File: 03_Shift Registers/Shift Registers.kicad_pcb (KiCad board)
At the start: 2 copper layers, 100 x 100 mm, 51 parts, among them J1 Data bus, J2 Alu-X bus, J3 Alu-Y bus, J4 Input 1, J5 Input 2, U1 74LS194, U10 74LS245, U2 74LS245, U3 74LS194, U4 74LS194, U5 74LS245, U6 74LS194, U7 74LS245, U8 74LS245, U9 74LS245

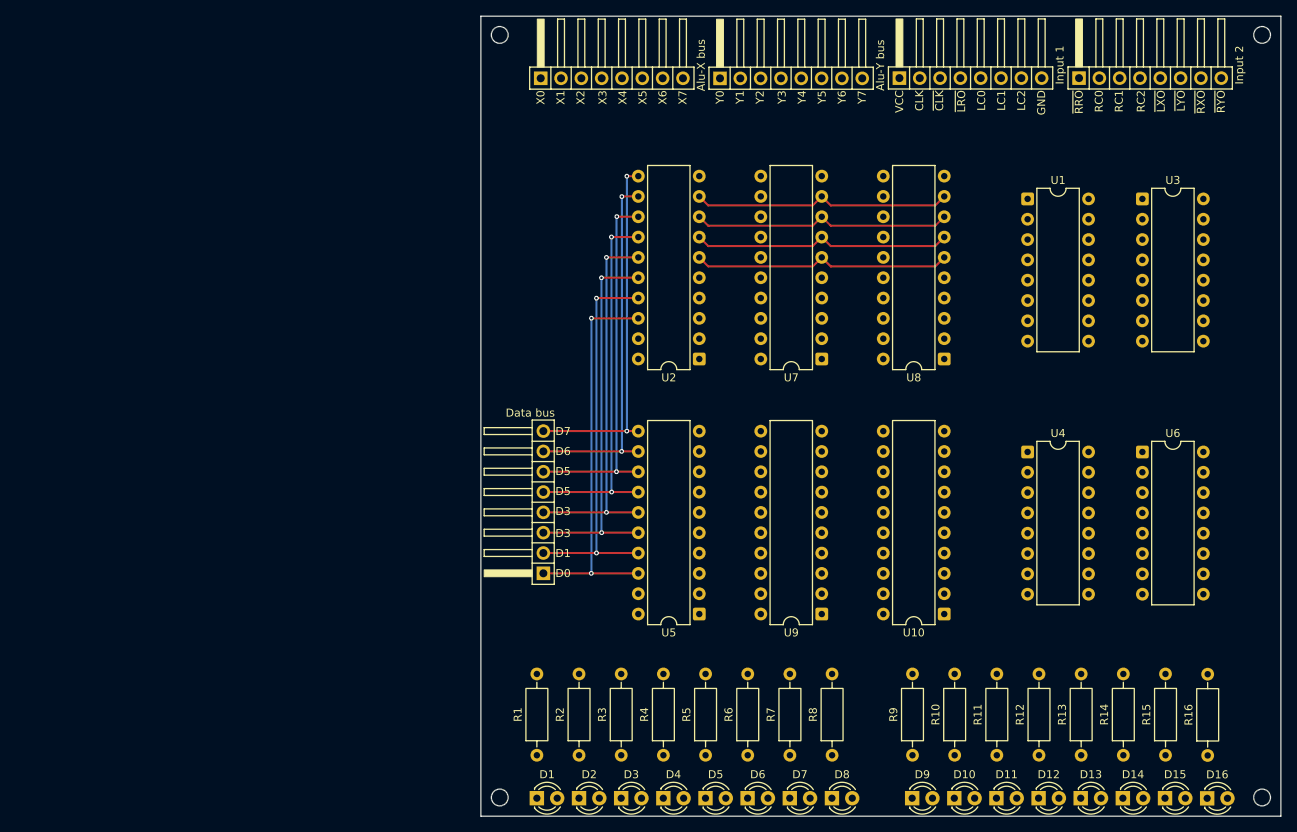
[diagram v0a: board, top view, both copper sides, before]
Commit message: Alu control and modules completed, as well as Stack pointer module
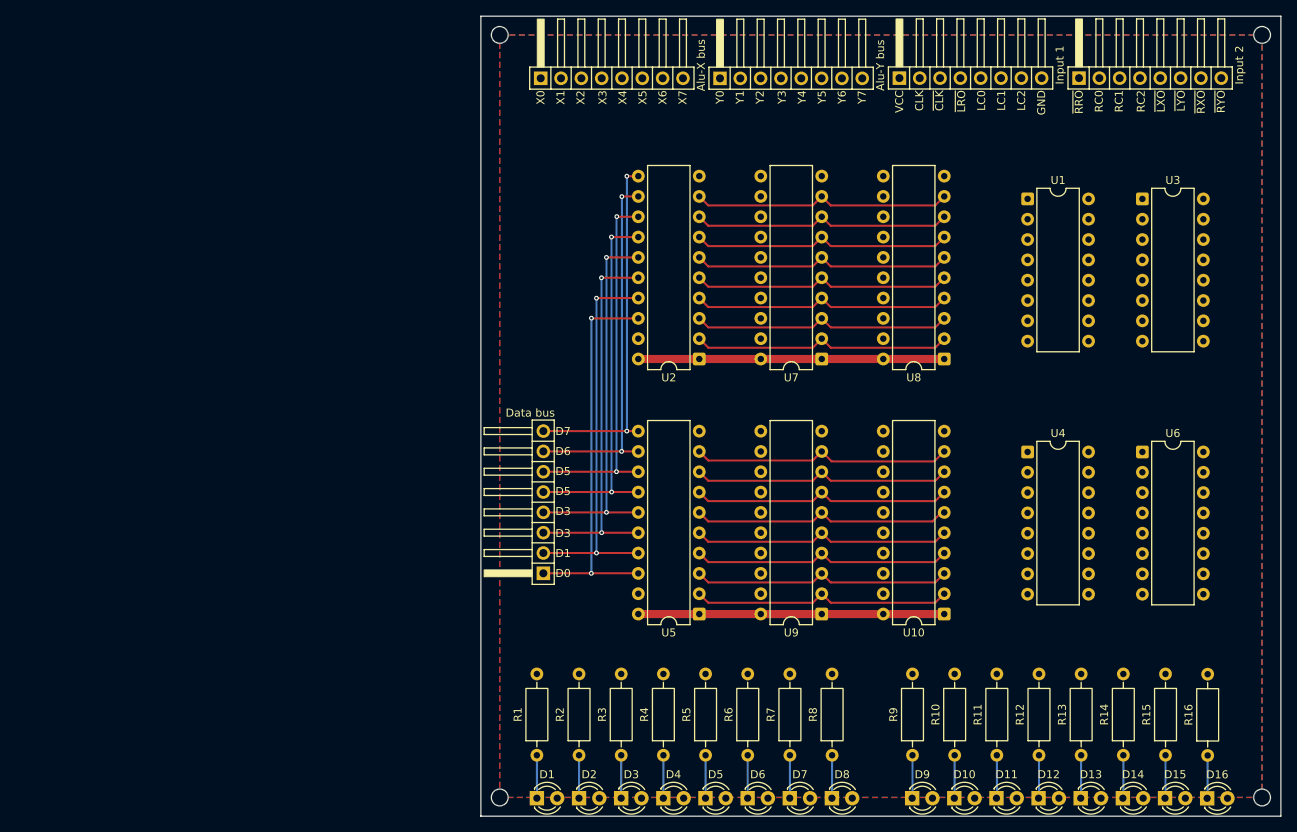
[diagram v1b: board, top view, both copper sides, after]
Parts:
- D1, D10, D11, D12, D13, D14, D15, D16, D2, D3, D4, D5, D6, D7, D8, D9: value LED -> RED
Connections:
- net /CLK renamed CLK
- net /D0 renamed D0
- net /D1 renamed D1
- net /D2 renamed D2
- net /D3 renamed D3
- net /D4 renamed D4
- net /D5 renamed D5
- net /D6 renamed D6
- net /D7 renamed D7
- net /GND renamed GND
- net /LC0 renamed LC0
- net /LC1 renamed LC1
- net /LC2 renamed LC2
- net /RC0 renamed RC0
- net /RC1 renamed RC1
- net /RC2 renamed RC2
- net /VCC renamed VCC
- net /X0 renamed X0
- net /X1 renamed X1
- net /X2 renamed X2
- net /X3 renamed X3
- net /X4 renamed X4
- net /X5 renamed X5
- net /X6 renamed X6
- net /X7 renamed X7
- net /Y0 renamed Y0
- net /Y1 renamed Y1
- net /Y2 renamed Y2
- net /Y3 renamed Y3
- net /Y4 renamed Y4
- net /Y5 renamed Y5
- net /Y6 renamed Y6
- net /Y7 renamed Y7
- net /~{CLK} renamed ~{CLK}
- net /~{LRO} renamed ~{LRO}
- net /~{LXO} renamed ~{LXO}
- net /~{LYO} renamed ~{LYO}
- net /~{RRO} renamed ~{RRO}
- net /~{RXO} renamed ~{RXO}
- net /~{RYO} renamed ~{RYO}
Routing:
- net VCC: track 0.00 -> 76.5 mm
- net /Alu selector R-X/Q4: track 0.00 -> 33.0 mm
- net /Alu selector R-X/Q7: track 0.00 -> 32.6 mm
- net /Alu selector R-X/Q6: track 0.00 -> 32.5 mm
- net /Alu selector R-X/Q5: track 0.00 -> 32.5 mm
- net /Alu selector R-X/Q3: track 0.00 -> 32.5 mm
- net /Alu selector R-X/Q2: track 0.00 -> 32.5 mm
- net /Alu selector R-X/Q1: track 0.00 -> 32.5 mm
- net /Alu selector R-X/Q0: track 0.00 -> 32.5 mm
- net /Alu selector L-X/Q3: track 0.00 -> 32.5 mm
- net /Alu selector L-X/Q2: track 0.00 -> 32.5 mm
- net /Alu selector L-X/Q1: track 0.00 -> 32.5 mm
- net /Alu selector L-X/Q0: track 0.00 -> 32.5 mm
- net Net-(D15-K): track 0.00 -> 5.40 mm
- net Net-(D14-K): track 0.00 -> 5.39 mm
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- added copper zone on B.Cu, net GND
- added copper zone on F.Cu, net GND

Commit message: Last revision of the cpu, all boards have been ordered. Implementation to be tested and documented in following commits.
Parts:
- removed the U7 at (93.6, 86.0)
- removed the U9 at (93.6, 117.9)
- added U1: 74LS139, Package_DIP:DIP-16_W7.62mm, F.Cu at (19.2, 94.0)
- added U11: 74LS245, Package_DIP:DIP-20_W7.62mm, F.Cu at (6.47, 94.0)
- added U12: 74LS245, Package_DIP:DIP-20_W7.62mm, F.Cu at (-6.31, 65.1)
- added U13: 74LS245, Package_DIP:DIP-20_W7.62mm, F.Cu at (19.2, 65.1)
- U2: value 74LS245 -> 74LS00; footprint Package_DIP:DIP-20_W7.62mm -> Package_DIP:DIP-14_W7.62mm
- moved U10 117.7 mm to (-6.31, 94.0), turned to 0 degrees
- moved U5 89.1 mm to (6.47, 65.1), turned to 0 degrees
- moved U8 79.7 mm to (32.0, 65.1), turned to 0 degrees
- moved U2 48.9 mm to (30.0, 94.0), turned to 0 degrees
- renumbered R8 to R10, R9 to R11, R10 to R12, R11 to R13, R12 to R14, R13 to R15, R14 to R16, R15 to R17, R16 to R18, R1 to R3, R2 to R4, R3 to R5, R4 to R6, R5 to R7, R6 to R8, R7 to R9, U1 to U4, U3 to U6, U4 to U7, U6 to U9
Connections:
- J4 pad 7: LC2 -> LCL
- J5 pad 4: RC2 -> RCL
- U10 pad 11: Y7 -> X7
- U10 pad 12: Y6 -> X6
- U10 pad 13: Y5 -> X5
- U10 pad 14: Y4 -> X4
- U10 pad 15: Y3 -> X3
- U10 pad 16: Y2 -> X2
- U10 pad 17: Y1 -> X1
- U10 pad 18: Y0 -> X0
- U10 pad 19: ~{RYO} -> ~{LXO}
- U10 pad 2: /Alu selector R-X/Q0 -> /Alu selector L-X/Q0
- U10 pad 3: /Alu selector R-X/Q1 -> /Alu selector L-X/Q1
- U10 pad 4: /Alu selector R-X/Q2 -> /Alu selector L-X/Q2
- U10 pad 5: /Alu selector R-X/Q3 -> /Alu selector L-X/Q3
- U10 pad 6: /Alu selector R-X/Q4 -> /Alu selector L-X/Q4
- U10 pad 7: /Alu selector R-X/Q5 -> /Alu selector L-X/Q5
- U10 pad 8: /Alu selector R-X/Q6 -> /Alu selector L-X/Q6
- U10 pad 9: /Alu selector R-X/Q7 -> /Alu selector L-X/Q7
- U2 pad 1: VCC -> Net-(U1A-O1)
- U2 pad 10: GND -> ~{RRI}
- U2 pad 11: D7 -> /Shift register R/S1
- U2 pad 12: D6 -> ~{RRI}
- U2 pad 13: D5 -> Net-(U1B-O2)
- U2 pad 14: D4 -> VCC
- U2 pad 2: /Alu selector L-X/Q0 -> ~{LRI}
- U2 pad 3: /Alu selector L-X/Q1 -> /Shift register L/S0
- U2 pad 4: /Alu selector L-X/Q2 -> ~{LRI}
- U2 pad 5: /Alu selector L-X/Q3 -> Net-(U1A-O2)
- U2 pad 6: /Alu selector L-X/Q4 -> /Shift register L/S1
- U2 pad 7: /Alu selector L-X/Q5 -> GND
- U2 pad 8: /Alu selector L-X/Q6 -> /Shift register R/S0
- U2 pad 9: /Alu selector L-X/Q7 -> Net-(U1B-O1)
- U4 pad 1: LC2 -> /Shift register L/~{MR}
- U4 pad 10: LC1 -> /Shift register L/S1
- U4 pad 9: LC0 -> /Shift register L/S0
- U5 pad 19: ~{RRO} -> ~{LRO}
- U5 pad 2: /Alu selector R-X/Q0 -> /Alu selector L-X/Q0
- U5 pad 3: /Alu selector R-X/Q1 -> /Alu selector L-X/Q1
- U5 pad 4: /Alu selector R-X/Q2 -> /Alu selector L-X/Q2
- U5 pad 5: /Alu selector R-X/Q3 -> /Alu selector L-X/Q3
- U5 pad 6: /Alu selector R-X/Q4 -> /Alu selector L-X/Q4
- U5 pad 7: /Alu selector R-X/Q5 -> /Alu selector L-X/Q5
- U5 pad 8: /Alu selector R-X/Q6 -> /Alu selector L-X/Q6
- U5 pad 9: /Alu selector R-X/Q7 -> /Alu selector L-X/Q7
- U6 pad 1: LC2 -> /Shift register L/~{MR}
- U6 pad 10: LC1 -> /Shift register L/S1
- U6 pad 9: LC0 -> /Shift register L/S0
- U7 pad 1: RC2 -> /Shift register R/~{MR}
- U7 pad 10: RC1 -> /Shift register R/S1
- U7 pad 9: RC0 -> /Shift register R/S0
- U8 pad 11: Y7 -> D7
- U8 pad 12: Y6 -> D6
- U8 pad 13: Y5 -> D5
- U8 pad 14: Y4 -> D4
- U8 pad 15: Y3 -> D3
- U8 pad 16: Y2 -> D2
- U8 pad 17: Y1 -> D1
- U8 pad 18: Y0 -> D0
- U8 pad 19: ~{LYO} -> ~{RRO}
- U8 pad 2: /Alu selector L-X/Q0 -> /Alu selector R-X/Q0
- U8 pad 3: /Alu selector L-X/Q1 -> /Alu selector R-X/Q1
- U8 pad 4: /Alu selector L-X/Q2 -> /Alu selector R-X/Q2
- U8 pad 5: /Alu selector L-X/Q3 -> /Alu selector R-X/Q3
- U8 pad 6: /Alu selector L-X/Q4 -> /Alu selector R-X/Q4
- U8 pad 7: /Alu selector L-X/Q5 -> /Alu selector R-X/Q5
- U8 pad 8: /Alu selector L-X/Q6 -> /Alu selector R-X/Q6
- U8 pad 9: /Alu selector L-X/Q7 -> /Alu selector R-X/Q7
- U9 pad 1: RC2 -> /Shift register R/~{MR}
- U9 pad 10: RC1 -> /Shift register R/S1
- U9 pad 9: RC0 -> /Shift register R/S0
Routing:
- net VCC: track 76.5 -> 0.00 mm
- net D0: track 49.6 -> 5.99 mm, vias 2 -> 0
- net D1: track 49.0 -> 6.64 mm, vias 2 -> 0
- net D2: track 48.4 -> 7.29 mm, vias 2 -> 0
- net D3: track 47.7 -> 7.89 mm, vias 2 -> 0
- net D4: track 47.1 -> 8.54 mm, vias 2 -> 0
- net D5: track 46.5 -> 9.14 mm, vias 2 -> 0
- net D6: track 45.8 -> 9.79 mm, vias 2 -> 0
- net D7: track 45.2 -> 10.4 mm, vias 2 -> 0
- net /Alu selector R-X/Q4: track 33.0 -> 0.00 mm
- net /Alu selector R-X/Q7: track 32.6 -> 0.00 mm
- net /Alu selector R-X/Q6: track 32.5 -> 0.00 mm
- net /Alu selector R-X/Q5: track 32.5 -> 0.00 mm
- net /Alu selector R-X/Q3: track 32.5 -> 0.00 mm
- net /Alu selector R-X/Q2: track 32.5 -> 0.00 mm
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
